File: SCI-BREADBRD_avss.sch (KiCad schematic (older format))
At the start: 21 parts

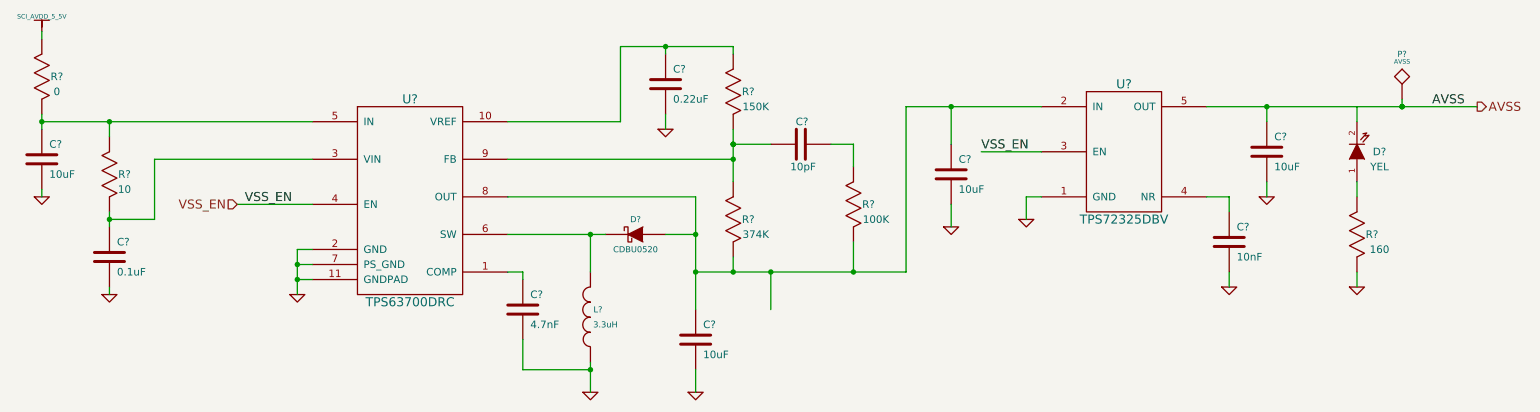
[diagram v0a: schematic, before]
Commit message: Fixed the footprint properties of various parts throughout the schematic to make sure they are all point to valid footprints.
Added SCI-BREADBRD.cmp to specify which footprints should be used for
each part.

Added netlists to the .gitignore as those can be generated easily in
eeschema.
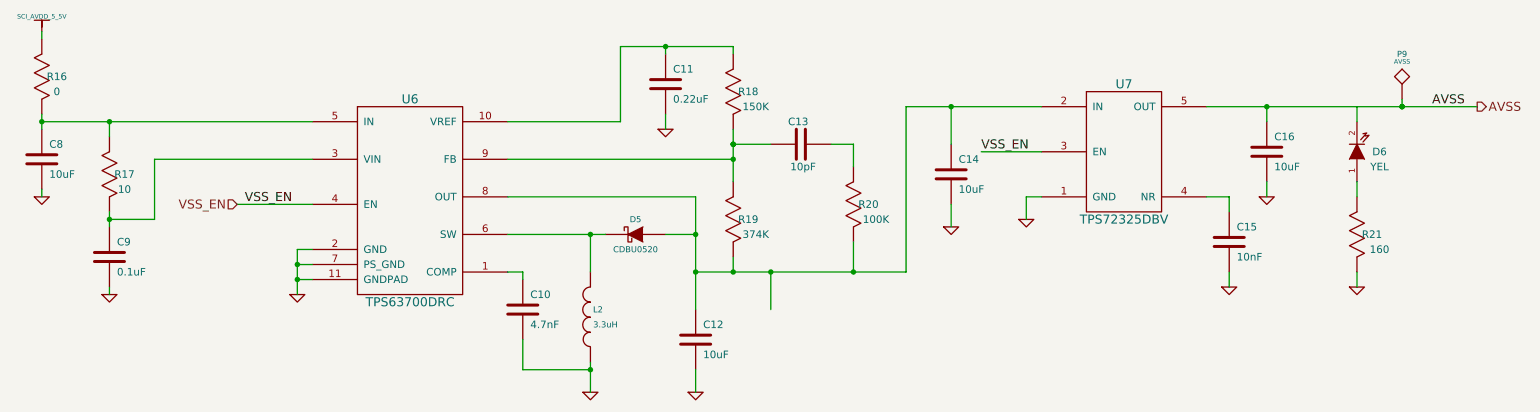
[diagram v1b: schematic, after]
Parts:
- C10, C11, C13, C15, C9: renamed from C?; footprint SM0402 -> 0402
- C12, C14, C16, C8: renamed from C?; footprint SM0603 -> 0603
- D5: renamed from D?; footprint SM0603 -> 0603
- D6: renamed from D?; footprint SM0402 -> 0402
- L2: renamed from L?; footprint SM0806 -> 0806
- R16: renamed from R?; footprint SM0603 -> 0603
- R17, R18, R19, R20, R21: renamed from R?; footprint SM0402 -> 0402
- gave numbers to parts that had none: 3
